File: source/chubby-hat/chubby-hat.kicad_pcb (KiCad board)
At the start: 2 copper layers, 143.5 x 91.4 mm, 175 parts, among them J1 HUB75, J10 Conn_ARM_JTAG_SWD_10, J11 Conn_ARM_JTAG_SWD_10, J12 TC2030, J13 5V, J14 5V, J15 5V, J16 5V, J17 USB_C_Receptacle_USB2.0, J18 Conn_01x04, J19 Conn_01x02, J2 HUB75, J20 Conn_01x02, J3 HUB75, J4 HUB75, J5 HUB75, J6 HUB75, J7 HUB75, J8 HUB75, J9 UART, Q1 AO3401A, SW1 RUN, SW2 BOOT, U1 AMS1117-3.3, U2 RP2040-Zero, U3 USBLC6-2SC6, U4 P25Q40H-SSH-IT, U5 RP2040, Y1 12M

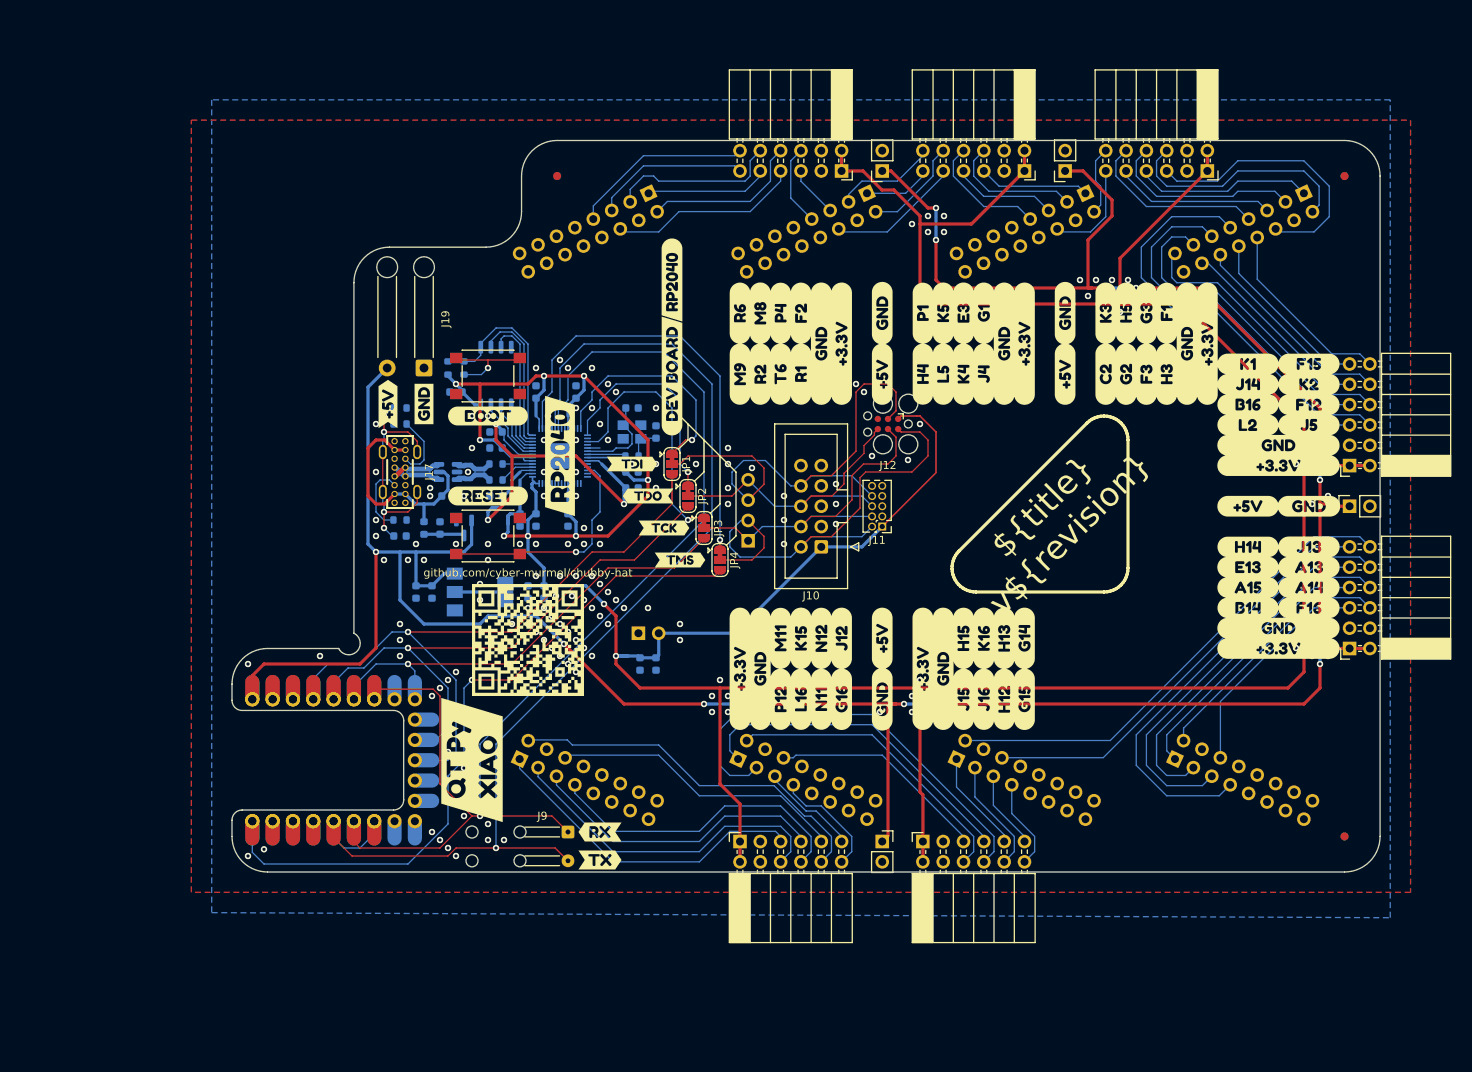
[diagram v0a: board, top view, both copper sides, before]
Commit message: added connectors for v8.0; improved power layout
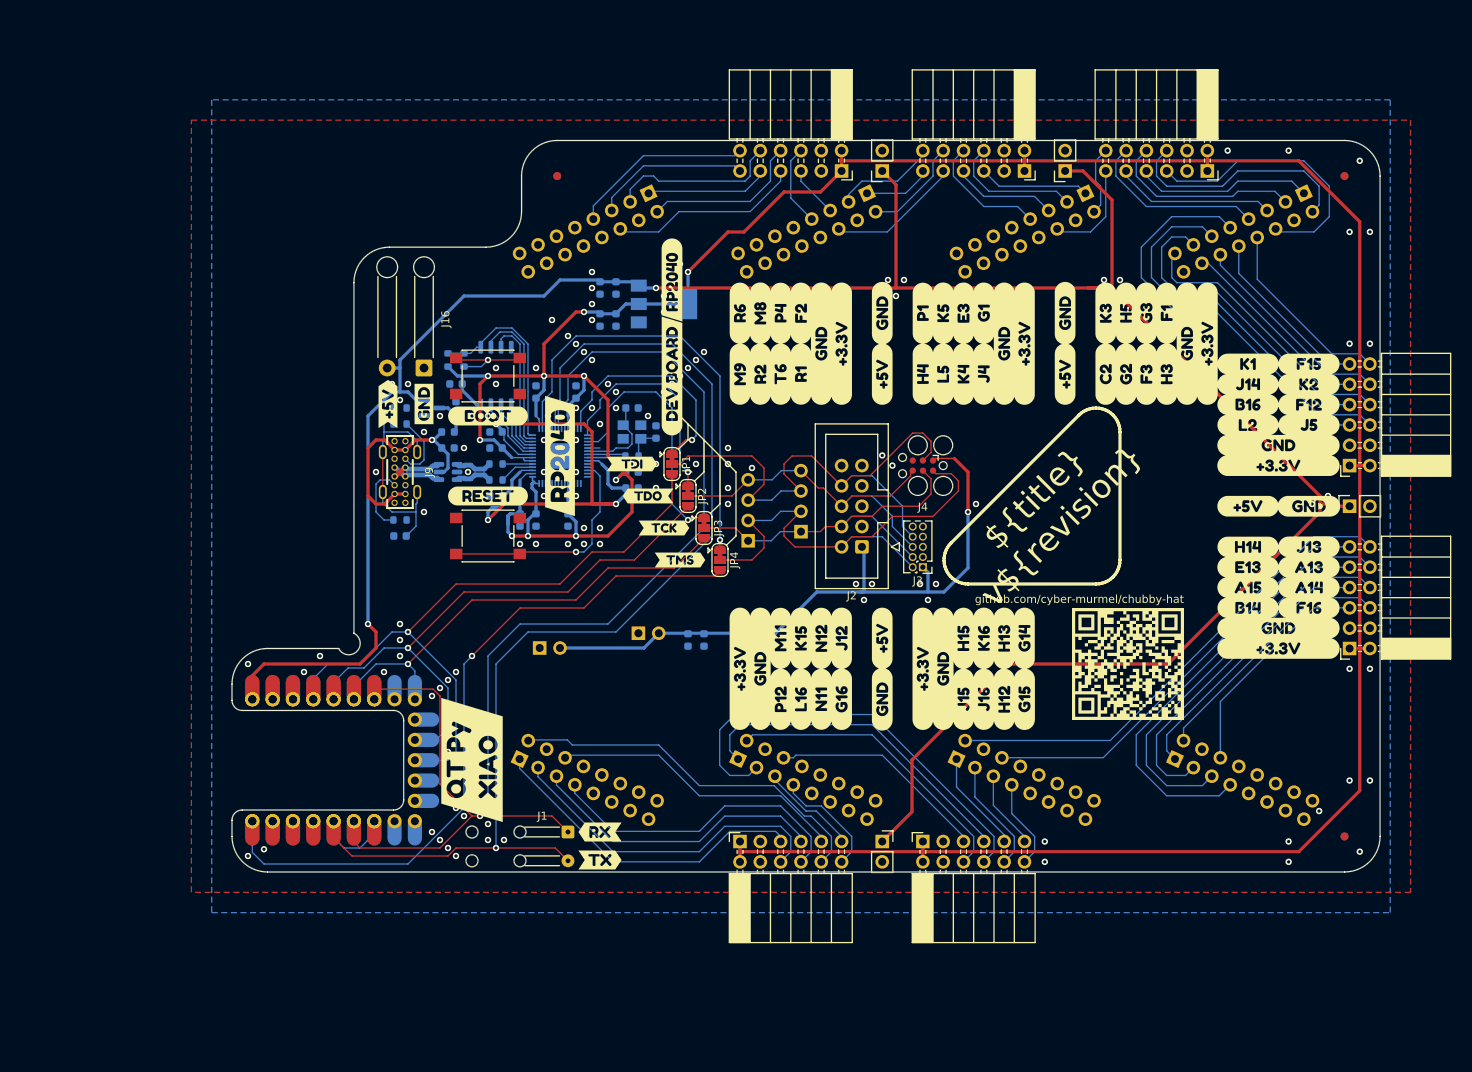
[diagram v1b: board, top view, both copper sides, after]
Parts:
- removed the NT1 at (176.0, 100.0)
- added J14: v8.0, Connector_PinHeader_2.54mm:PinHeader_1x04_P2.54mm_Vertical, B.Cu at (198.1, 84.5)
- added J20: V8.0, Connector_PinHeader_2.54mm:PinHeader_1x02_P2.54mm_Vertical, B.Cu at (165.5, 99.0)
- J13: renamed from J18; value Conn_01x04 -> v7.0
- J19: renamed from J20; value Conn_01x02 -> V7.0
- moved QR***** 75.1 mm to (239.0, 101.0)
- moved C1 44.4 mm to (175.0, 54.0)
- moved C2 44.4 mm to (173.0, 54.0)
- moved U1 42.7 mm to (181.0, 56.0)
- moved C4 35.7 mm to (175.0, 58.0)
- moved C3 34.7 mm to (173.0, 58.0)
- moved Q1 15.5 mm to (152.0, 69.0), turned to 0 degrees
- moved C6 15.1 mm to (155.0, 69.0)
- moved FB1 12.4 mm to (154.0, 72.0), turned to 180 degrees
- moved C8 8.54 mm to (186.0, 98.0)
- moved J3 7.18 mm to (213.4, 88.9)
- moved J4 6.79 mm to (213.4, 76.2)
- moved C7 6.00 mm to (154.0, 74.0)
- moved J2 5.08 mm to (205.7, 86.4)
- moved C10 5.00 mm to (184.0, 98.0)
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- renumbered C9 to C10, C10 to C12, C11 to C13, C12 to C14, C13 to C15, C14 to C16, C15 to C17, C16 to C18, C17 to C19, C18 to C20, C19 to C21, C20 to C22, C21 to C23, C22 to C24, J9 to J1, J5 to J10, J4 to J11, J6 to J12, J3 to J15, J19 to J16, J7 to J17, J2 to J18, J10 to J2, J8 to J21, J1 to J22, J11 to J3, J12 to J4, J13 to J5, J14 to J6, J15 to J7, J16 to J8, J17 to J9, NT2 to NT1, NT3 to NT2
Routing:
- net +3V3: track 455.2 -> 407.8 mm
- net +5V: track 357.7 -> 310.7 mm, vias 14 -> 2
- net VDD: track 60.5 -> 81.9 mm, vias 0 -> 1
- net /RP2040/DVDD: track 47.3 -> 59.4 mm
- net /RP2040/GPIO5: track 148.1 -> 154.5 mm
- net /RP2040/GPIO4: track 138.9 -> 145.3 mm
- net /JTAG.TDO: track 41.4 -> 46.1 mm
- net /JTAG.TCK: track 44.0 -> 46.3 mm
- net /JTAG_{DevBoard}.TMS: track 85.7 -> 87.4 mm
- net /JTAG.TMS: track 64.2 -> 62.7 mm
- net /RP2040/QSPI.~{CS}: track 25.3 -> 24.3 mm
- net /RP2040/~{USB_BOOT}: track 12.5 -> 11.5 mm
- net /JTAG.TDI: track 68.4 -> 69.1 mm
- net VBUS: track 29.1 -> 28.5 mm, vias 0 -> 1
- net Earth: track 29.3 -> 29.2 mm, vias 4 -> 0
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
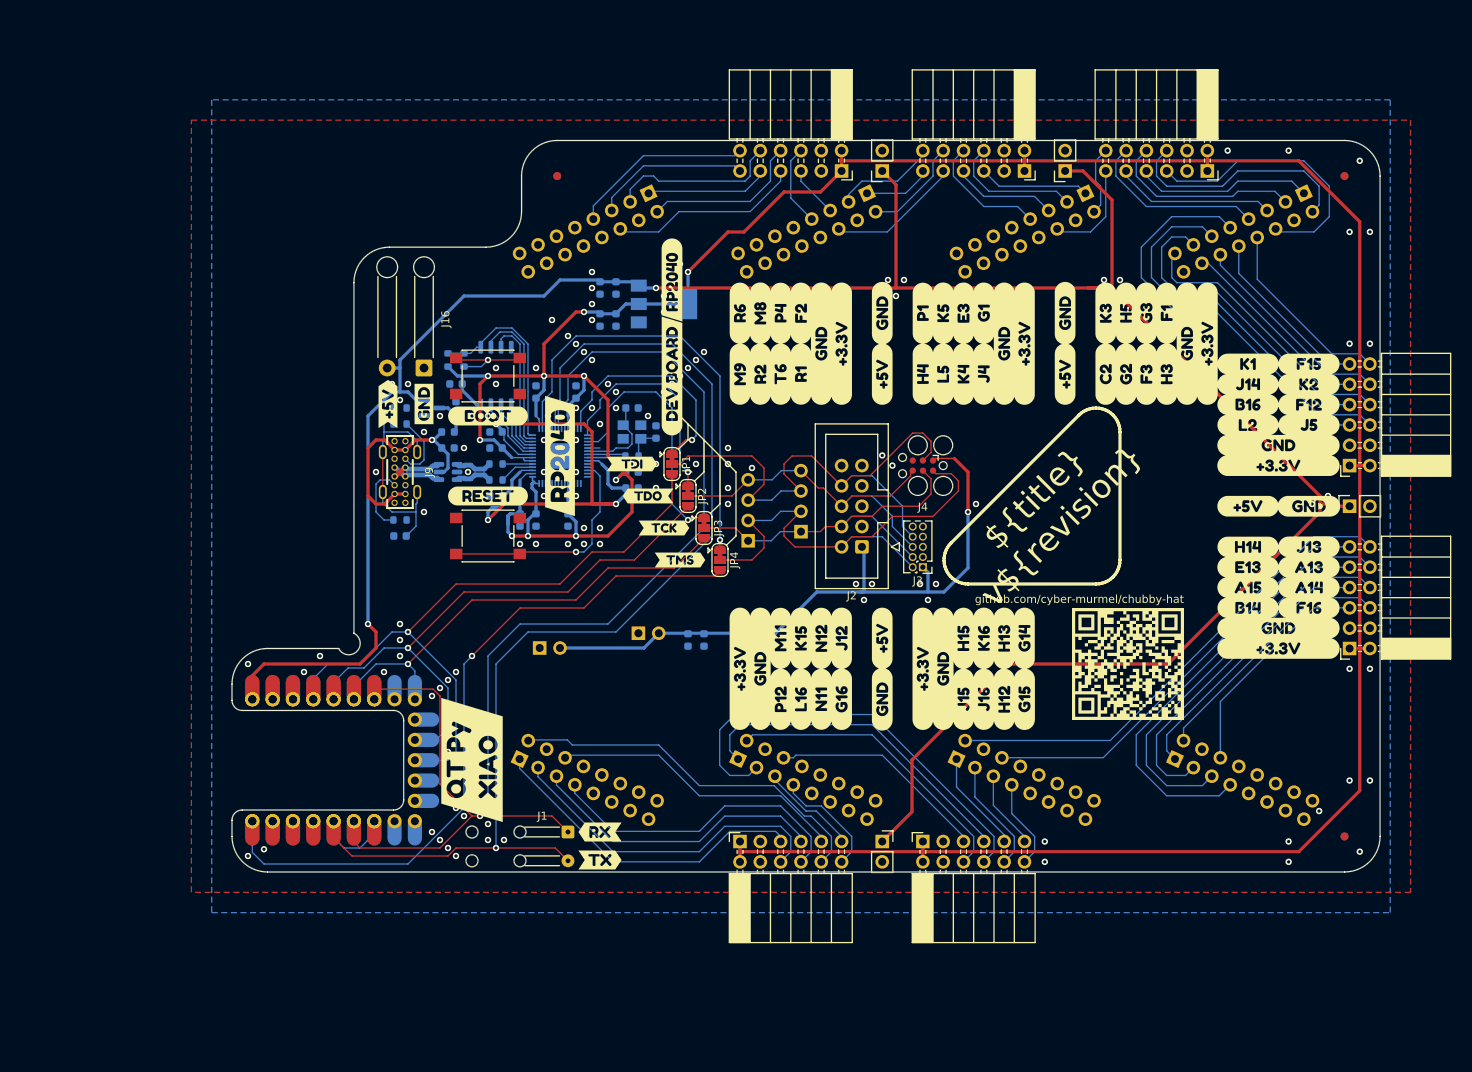
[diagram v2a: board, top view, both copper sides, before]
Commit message: add test points and leds - closes #1; add fuse - closes #4; add silk screen art
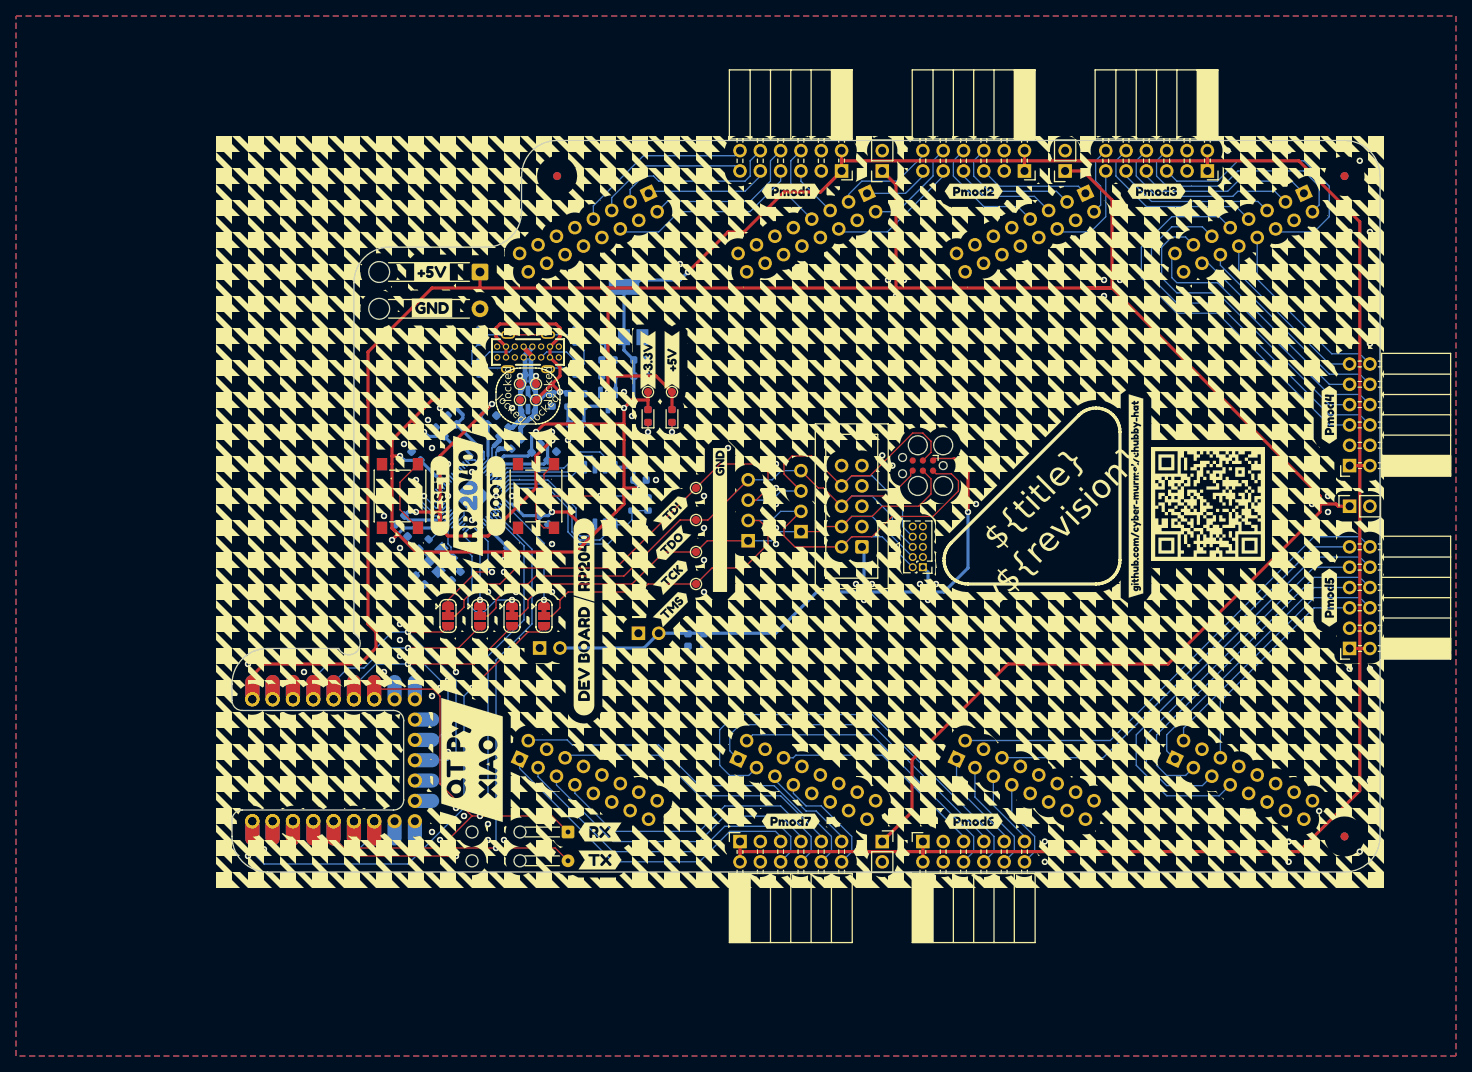
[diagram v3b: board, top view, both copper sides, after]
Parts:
- removed kibuzzard-63D6B0C3: G***, kibuzzard-63D6B0C3
- removed kibuzzard-63D6B0C7: G***, kibuzzard-63D6B0C7
- removed kibuzzard-63D6B0CA: G***, kibuzzard-63D6B0CA
- removed kibuzzard-63D6B0D2: G***, kibuzzard-63D6B0D2
- removed kibuzzard-63D6B166: G***, kibuzzard-63D6B166
- removed kibuzzard-63D6C259 (x7): G***, kibuzzard-63D6C259
- removed kibuzzard-63D6C27C (x7): G***, kibuzzard-63D6C27C
- removed kibuzzard-63D6CE6B: G***, kibuzzard-63D6CE6B
- removed kibuzzard-63D6CE73: G***, kibuzzard-63D6CE73
- removed kibuzzard-63D6CE81: G***, kibuzzard-63D6CE81
- removed kibuzzard-63D6CE8F: G***, kibuzzard-63D6CE8F
- removed kibuzzard-63D6CE96: G***, kibuzzard-63D6CE96
- removed kibuzzard-63D6CEA2: G***, kibuzzard-63D6CEA2
- removed kibuzzard-63D6CEA8: G***, kibuzzard-63D6CEA8
- removed kibuzzard-63D6CEAE: G***, kibuzzard-63D6CEAE
- removed kibuzzard-63D6CEDA (x4): G***, kibuzzard-63D6CEDA
- removed kibuzzard-63D6CEDF (x4): G***, kibuzzard-63D6CEDF
- removed kibuzzard-63D6CF31: G***, kibuzzard-63D6CF31
- removed kibuzzard-63D6CF38: G***, kibuzzard-63D6CF38
- removed kibuzzard-63D6CF3E: G***, kibuzzard-63D6CF3E
- removed kibuzzard-63D6CF44: G***, kibuzzard-63D6CF44
- removed kibuzzard-63D6CF49: G***, kibuzzard-63D6CF49
- removed kibuzzard-63D6CF4E: G***, kibuzzard-63D6CF4E
- removed kibuzzard-63D6CF54: G***, kibuzzard-63D6CF54
- removed kibuzzard-63D6CF58: G***, kibuzzard-63D6CF58
- removed kibuzzard-63D6CF83: G***, kibuzzard-63D6CF83
- removed kibuzzard-63D6CF88: G***, kibuzzard-63D6CF88
- removed kibuzzard-63D6CF8C: G***, kibuzzard-63D6CF8C
- removed kibuzzard-63D6CF91: G***, kibuzzard-63D6CF91
- removed kibuzzard-63D6CF96: G***, kibuzzard-63D6CF96
- removed kibuzzard-63D6CF9A: G***, kibuzzard-63D6CF9A
- removed kibuzzard-63D6CF9E: G***, kibuzzard-63D6CF9E
- removed kibuzzard-63D6CFA2: G***, kibuzzard-63D6CFA2
- removed kibuzzard-63D6D057: G***, kibuzzard-63D6D057
- removed kibuzzard-63D6D06E: G***, kibuzzard-63D6D06E
- removed kibuzzard-63D6D07B: G***, kibuzzard-63D6D07B
- removed kibuzzard-63D6D081: G***, kibuzzard-63D6D081
- removed kibuzzard-63D6D088: G***, kibuzzard-63D6D088
- removed kibuzzard-63D6D08F: G***, kibuzzard-63D6D08F
- removed kibuzzard-63D6D098: G***, kibuzzard-63D6D098
- removed kibuzzard-63D6D09C: G***, kibuzzard-63D6D09C
- removed kibuzzard-63D6D0D6: G***, kibuzzard-63D6D0D6
- removed kibuzzard-63D6D0DD: G***, kibuzzard-63D6D0DD
- removed kibuzzard-63D6D0E4: G***, kibuzzard-63D6D0E4
- removed kibuzzard-63D6D0EA: G***, kibuzzard-63D6D0EA
- removed kibuzzard-63D6D0F4: G***, kibuzzard-63D6D0F4
- removed kibuzzard-63D6D0FB: G***, kibuzzard-63D6D0FB
- removed kibuzzard-63D6D103: G***, kibuzzard-63D6D103
- removed kibuzzard-63D6D10E: G***, kibuzzard-63D6D10E
- removed kibuzzard-63D6D1C6: G***, kibuzzard-63D6D1C6
- removed kibuzzard-63D6D1CB: G***, kibuzzard-63D6D1CB
- removed kibuzzard-63D6D1D1: G***, kibuzzard-63D6D1D1
- removed kibuzzard-63D6D1D5: G***, kibuzzard-63D6D1D5
- removed kibuzzard-63D6D1DB: G***, kibuzzard-63D6D1DB
- removed kibuzzard-63D6D1E0: G***, kibuzzard-63D6D1E0
- removed kibuzzard-63D6D1E4: G***, kibuzzard-63D6D1E4
- removed kibuzzard-63D6D1E8: G***, kibuzzard-63D6D1E8
- removed kibuzzard-63D6D239: G***, kibuzzard-63D6D239
- removed kibuzzard-63D6D23D: G***, kibuzzard-63D6D23D
- removed kibuzzard-63D6D243: G***, kibuzzard-63D6D243
- removed kibuzzard-63D6D247: G***, kibuzzard-63D6D247
- removed kibuzzard-63D6D24E: G***, kibuzzard-63D6D24E
- removed kibuzzard-63D6D255: G***, kibuzzard-63D6D255
- removed kibuzzard-63D6D259: G***, kibuzzard-63D6D259
- removed kibuzzard-63D6D25E: G***, kibuzzard-63D6D25E
- added D1: LED, LED_SMD:LED_0603_1608Metric, F.Cu at (182.0, 70.0)
- added D2: LED, LED_SMD:LED_0603_1608Metric, F.Cu at (179.0, 70.0)
- added F1: 500mA, Resistor_SMD:R_0603_1608Metric, B.Cu at (169.0, 68.0)
- added R1: 1k, Resistor_SMD:R_0603_1608Metric, B.Cu at (182.0, 70.0)
- added R2: 1k, Resistor_SMD:R_0603_1608Metric, B.Cu at (179.0, 70.0)
- added TP1: +5V, TestPoint:TestPoint_Pad_D1.0mm, F.Cu at (182.0, 67.0)
- added TP10: TCK, TestPoint:TestPoint_Pad_D1.0mm, F.Cu at (185.0, 87.0)
- added TP11: locked, TestPoint:TestPoint_Pad_D1.0mm, F.Cu at (163.0, 68.0)
- added TP12: locked, TestPoint:TestPoint_Pad_D1.0mm, F.Cu at (165.0, 68.0)
- added TP13: locked, TestPoint:TestPoint_Pad_D1.0mm, F.Cu at (163.0, 66.0)
- added TP14: locked, TestPoint:TestPoint_Pad_D1.0mm, F.Cu at (165.0, 66.0)
- added TP2: +3.3V, TestPoint:TestPoint_Pad_D1.0mm, F.Cu at (179.0, 67.0)
- added TP3: GND, TestPoint:TestPoint_Pad_D1.0mm, F.Cu at (188.0, 83.0)
- added TP4: GND, TestPoint:TestPoint_Pad_D1.0mm, F.Cu at (188.0, 79.0)
- added TP5: GND, TestPoint:TestPoint_Pad_D1.0mm, F.Cu at (188.0, 91.0)
- added TP6: GND, TestPoint:TestPoint_Pad_D1.0mm, F.Cu at (188.0, 87.0)
- added TP7: TDO, TestPoint:TestPoint_Pad_D1.0mm, F.Cu at (185.0, 83.0)
- added TP8: TDI, TestPoint:TestPoint_Pad_D1.0mm, F.Cu at (185.0, 79.0)
- added TP9: TMS, TestPoint:TestPoint_Pad_D1.0mm, F.Cu at (185.0, 91.0)
- added kibuzzard-63E5252B: G***, kibuzzard-63E5252B, F.Cu at (152.0, 52.0)
- added kibuzzard-63E54109: G***, kibuzzard-63E54109, F.Cu at (182.0, 82.0)
- added kibuzzard-63E54112: G***, kibuzzard-63E54112, F.Cu at (182.0, 86.0)
- added kibuzzard-63E5411A: G***, kibuzzard-63E5411A, F.Cu at (182.0, 90.0)
- added kibuzzard-63E54120: G***, kibuzzard-63E54120, F.Cu at (182.0, 94.0)
- added kibuzzard-63E58302: G***, kibuzzard-63E58302, F.Cu at (182.0, 63.0)
- added kibuzzard-63E5830C: G***, kibuzzard-63E5830C, F.Cu at (179.0, 63.0)
- added kibuzzard-63E58321: G***, kibuzzard-63E58321, F.Cu at (188.0, 83.0)
- added kibuzzard-63E586AA: G***, kibuzzard-63E586AA, F.Cu at (196.8, 41.9)
- added kibuzzard-63E586B9: G***, kibuzzard-63E586B9, F.Cu at (219.7, 41.9)
- added kibuzzard-63E586CE: G***, kibuzzard-63E586CE, F.Cu at (242.6, 41.9)
- added kibuzzard-63E586D5: G***, kibuzzard-63E586D5, F.Cu at (264.2, 69.8)
- added kibuzzard-63E586DD: G***, kibuzzard-63E586DD, F.Cu at (264.2, 92.7)
- added kibuzzard-63E586E8: G***, kibuzzard-63E586E8, F.Cu at (219.7, 120.7)
- added kibuzzard-63E586F0: G***, kibuzzard-63E586F0, F.Cu at (196.8, 120.7)
- added kibuzzard-63E5907B: G***, kibuzzard-63E5907B, F.Cu at (240.0, 80.0)
- moved kibuzzard-63D6CBB9 36.7 mm to (171.0, 88.0)
- moved kibuzzard-63D6CBA0 36.7 mm to (171.0, 100.0)
- moved C12 34.8 mm to (150.5, 90.5), turned to -45 degrees
- moved locked 33.8 mm to (154.0, 95.0)
- moved C5 33.3 mm to (170.0, 60.0), turned to 90 degrees
- moved R7 30.8 mm to (179.0, 81.0), turned to -90 degrees
- moved C11 30.4 mm to (155.0, 90.0), turned to -135 degrees
- moved locked 30.0 mm to (158.0, 95.0)
- moved C15 29.3 mm to (148.0, 83.0), turned to -135 degrees
- moved Y1 28.8 mm to (153.0, 88.0), turned to 45 degrees
- moved C17 28.5 mm to (149.5, 84.5), turned to -135 degrees
- moved R10 28.2 mm to (151.0, 86.0), turned to 45 degrees
- moved R6 27.7 mm to (177.0, 81.0), turned to -90 degrees
- moved locked 26.4 mm to (162.0, 95.0)
- moved C10 25.9 mm to (178.0, 78.0), turned to 0 degrees
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- renumbered C12 to C10, C13 to C11, C14 to C12, C15 to C13, C16 to C14, C17 to C15, C18 to C16, C19 to C17, C20 to C18, C21 to C19, C22 to C20, C23 to C21, C24 to C22, C10 to C9, Pmod7 to Pmod5, Pmod5 to Pmod7, R8 to R10, R1 to R3, R2 to R4, R3 to R5, R4 to R6, R5 to R7, R6 to R8, R7 to R9, JP2 to locked, JP4 to locked, JP1 to locked, JP3 to locked
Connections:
- FB1 pad 2: VBUS -> /Type C USB 2.0/VBUS_F1
- J16 pad 1: GND -> +5V
- J16 pad 2: +5V -> GND
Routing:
- net /RP2040/GPIO4: track 145.3 -> 85.3 mm
- net /RP2040/GPIO5: track 154.5 -> 97.7 mm
- net /RP2040/GPIO0: track 55.1 -> 14.9 mm
- net /JTAG_{DevBoard}.TDI: track 80.7 -> 42.6 mm
- net /JTAG.TDI: track 69.1 -> 105.7 mm
- net /JTAG.TDO: track 46.1 -> 78.9 mm
- net +3V3: track 407.8 -> 440.1 mm
- net /JTAG_{DevBoard}.TDO: track 69.8 -> 37.6 mm
- net +5V: track 310.7 -> 341.6 mm, vias 2 -> 1
- net /JTAG_{DevBoard}.TCK: track 55.3 -> 26.7 mm
- net /JTAG.TCK: track 46.3 -> 74.1 mm
- net /JTAG_{DevBoard}.TMS: track 87.4 -> 60.2 mm
- net /JTAG.TMS: track 62.7 -> 89.4 mm
- net /RP2040/GPIO12: track 27.8 -> 10.4 mm
- net /RP2040/GPIO11: track 28.6 -> 13.7 mm
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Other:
- board text added: "CAP"
